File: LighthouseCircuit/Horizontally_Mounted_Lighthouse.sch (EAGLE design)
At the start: 23 parts

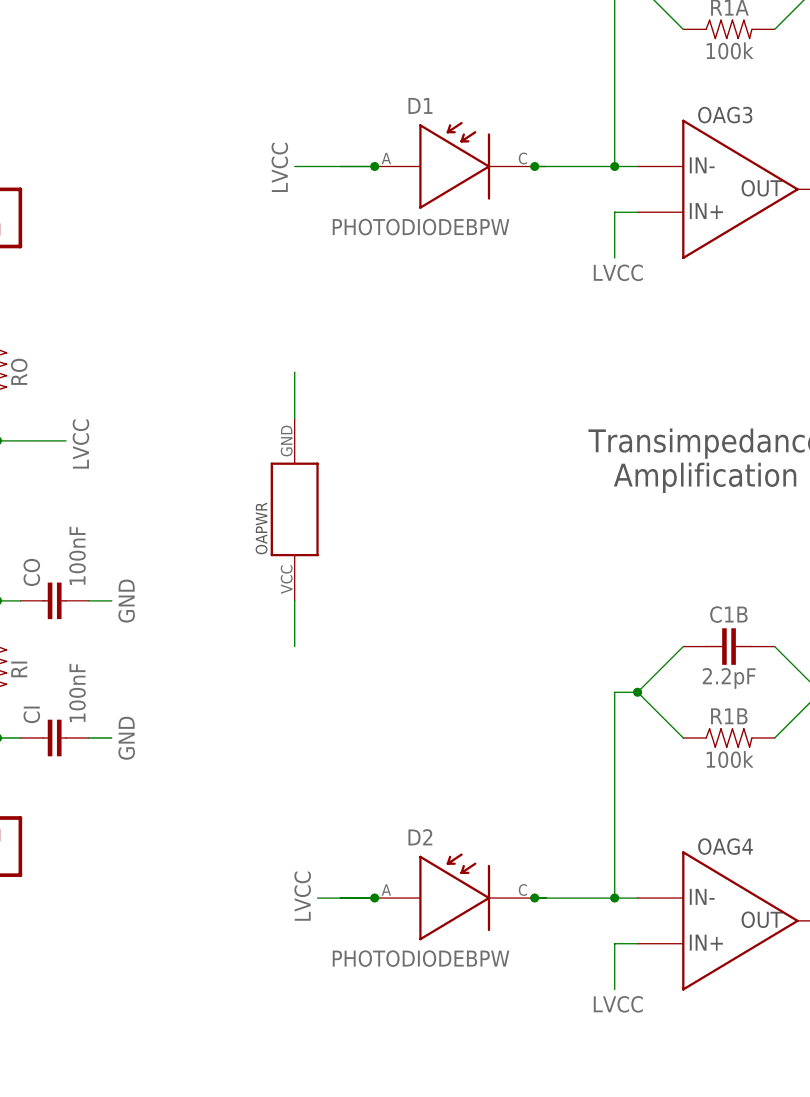
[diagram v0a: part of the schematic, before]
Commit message: Significantly stabilized the acceleration from full stop by slowing down the maximum speed. There is a physical limitation preventing them from accelerating any faster from full stop. Now that their wheels are offset, right turns cause the right wheel to lift up from the ground, creating error differences that the PID controllers are not setup to accommodate.
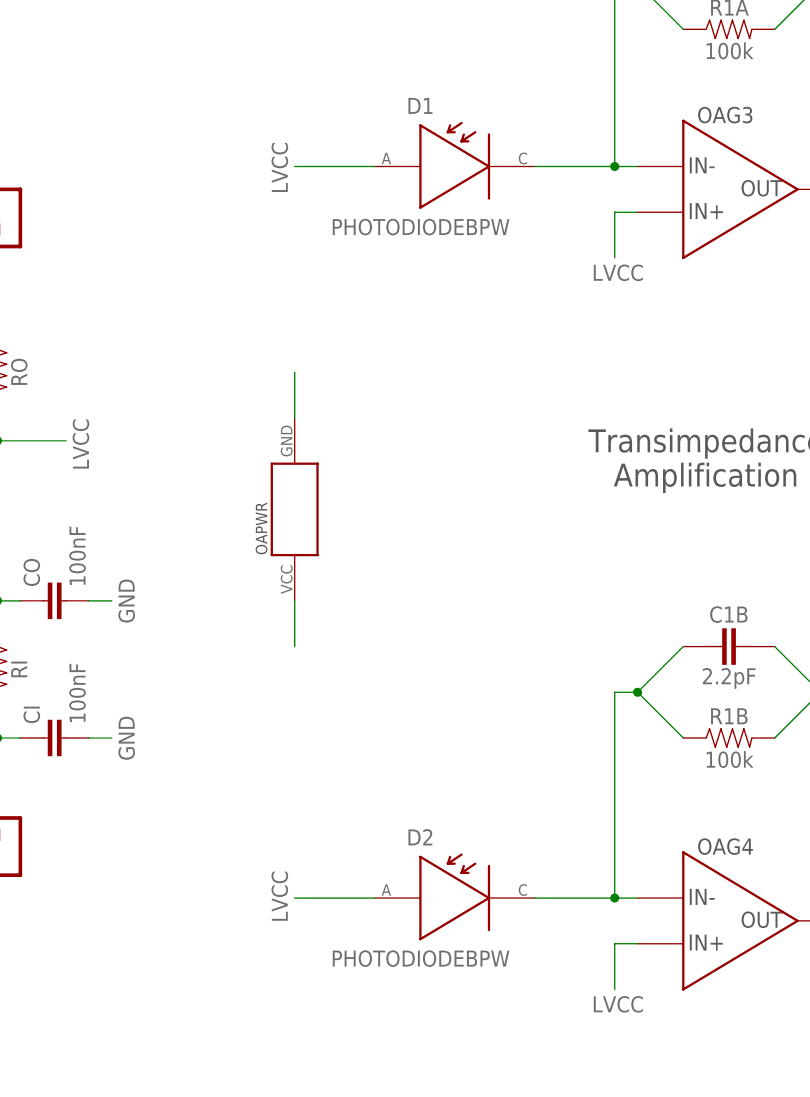
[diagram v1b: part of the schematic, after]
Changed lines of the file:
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@@
 </segment>
 <segment>
-<wire x1="157.48" y1="91.44" x2="161.29" y2="91.44" width="0.1524" layer="91"/>
 <label x="151.638" y="88.392" size="1.778" layer="95" rot="R90"/>
 <pinref part="D1" gate="G$1" pin="ANODE"/>
 <wire x1="161.29" y1="91.44" x2="152.4" y2="91.44" width="0.1524" layer="91"/>
-<junction x="161.29" y="91.44"/>
 </segment>
 <segment>
-<wire x1="157.48" y1="10.16" x2="161.29" y2="10.16" width="0.1524" layer="91"/>
-<label x="152.4" y="13.208" size="1.778" layer="95" rot="R270"/>
+<label x="149.86" y="13.208" size="1.778" layer="95" rot="R270"/>
 <pinref part="D2" gate="G$1" pin="ANODE"/>
-<wire x1="161.29" y1="10.16" x2="154.94" y2="10.16" width="0.1524" layer="91"/>
-<junction x="161.29" y="10.16"/>
+<wire x1="161.29" y1="10.16" x2="152.4" y2="10.16" width="0.1524" layer="91"/>
 </segment>
 <segment>
@@
 <wire x1="187.96" y1="91.44" x2="179.07" y2="91.44" width="0.1524" layer="91"/>
 <pinref part="R1A" gate="G$1" pin="1"/>
-<wire x1="179.07" y1="91.44" x2="180.34" y2="91.44" width="0.1524" layer="91"/>
 <wire x1="195.58" y1="106.68" x2="190.5" y2="111.76" width="0.1524" layer="91"/>
 <junction x="190.5" y="111.76"/>
@@
 <pinref part="OA" gate="G3" pin="IN-"/>
 <pinref part="D1" gate="G$1" pin="CATHODE"/>
-<junction x="179.07" y="91.44"/>
 </segment>
 </net>
 <net name="D1IN" class="0">
 <segment>
-<wire x1="180.34" y1="10.16" x2="179.07" y2="10.16" width="0.1524" layer="91"/>
 <wire x1="179.07" y1="10.16" x2="187.96" y2="10.16" width="0.1524" layer="91"/>
 <wire x1="190.5" y1="10.16" x2="187.96" y2="10.16" width="0.1524" layer="91"/>
@@
 <junction x="190.5" y="33.02"/>
 <pinref part="D2" gate="G$1" pin="CATHODE"/>
-<junction x="179.07" y="10.16"/>
 </segment>
 </net>
